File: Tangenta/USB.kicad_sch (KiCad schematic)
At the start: 29 parts, among them J12 907-211A1019D10200, J13 906-861A2116D10210, U8 USB2514B-I_M2, X1 X322524MOB4SI

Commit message: USB - current progress...
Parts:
- FB1: footprint footprint:L0805 -> Ferrite_Bead_100:Ferrite_Bead_100
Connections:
- net USB_U_N renamed USB_UP.N
- net USB_U_P renamed USB_UP.P
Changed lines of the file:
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@@
   (junction (at 38.862 173.609) (diameter 0) (color 0 0 0 0)
   )
-  (bus_entry (at 63.5 189.23) (size 2.54 2.54)
-    (stroke (width 0) (type default))
-  )
-  (bus_entry (at 54.61 189.23) (size 2.54 2.54)
+  (bus_entry (at 33.02 133.985) (size 2.54 2.54)
+    (stroke (width 0) (type default))
+  )
+  (bus_entry (at 41.91 133.985) (size 2.54 2.54)
+    (stroke (width 0) (type default))
+  )
+  (bus_entry (at 41.91 146.685) (size 2.54 2.54)
+    (stroke (width 0) (type default))
+  )
+  (bus_entry (at 33.02 146.685) (size 2.54 2.54)
     (stroke (width 0) (type default))
   )
@@
     (stroke (width 0) (type default))
   )
+  (bus (pts (xy 44.45 136.525) (xy 50.165 136.525))
+    (stroke (width 0) (type default))
+  )
   (wire (pts (xy 245.745 69.85) (xy 255.905 69.85))
     (stroke (width 0) (type default))
@@
     (stroke (width 0) (type default))
   )
-  (wire (pts (xy 45.72 186.055) (xy 60.325 186.055))
+  (wire (pts (xy 24.13 143.51) (xy 38.735 143.51))
+    (stroke (width 0) (type default))
+  )
+  (wire (pts (xy 55.118 163.83) (xy 55.118 166.37))
+    (stroke (width 0) (type default))
+  )
+  (wire (pts (xy 245.745 72.39) (xy 255.905 72.39))
+    (stroke (width 0) (type default))
+  )
+  (wire (pts (xy 167.6402 90.17) (xy 201.295 90.17))
+    (stroke (width 0) (type default))
+  )
+  (wire (pts (xy 29.464 182.88) (xy 36.449 182.88))
+    (stroke (width 0) (type default))
+  )
+  (wire (pts (xy 63.5 59.69) (xy 71.12 59.69))
+    (stroke (width 0) (type default))
+  )
+  (wire (pts (xy 62.611 163.83) (xy 62.611 166.37))
+    (stroke (width 0) (type default))
+  )
+  (wire (pts (xy 71.12 62.23) (xy 33.655 62.23))
     (stroke (width 0) (type default))
   )
@@
     (stroke (width 0) (type default))
   )
-  (wire (pts (xy 55.118 163.83) (xy 55.118 166.37))
-    (stroke (width 0) (type default))
-  )
-  (wire (pts (xy 245.745 72.39) (xy 255.905 72.39))
-    (stroke (width 0) (type default))
-  )
-  (wire (pts (xy 167.6402 90.17) (xy 201.295 90.17))
-    (stroke (width 0) (type default))
-  )
-  (wire (pts (xy 29.464 182.88) (xy 36.449 182.88))
-    (stroke (width 0) (type default))
-  )
-  (wire (pts (xy 63.5 59.69) (xy 71.12 59.69))
-    (stroke (width 0) (type default))
-  )
-  (wire (pts (xy 62.611 163.83) (xy 62.611 166.37))
-    (stroke (width 0) (type default))
-  )
-  (wire (pts (xy 71.12 62.23) (xy 33.655 62.23))
-    (stroke (width 0) (type default))
-  )
   (wire (pts (xy 194.945 87.63) (xy 186.055 87.63))
     (stroke (width 0) (type default))
@@
     (stroke (width 0) (type default))
   )
-  (wire (pts (xy 63.5 189.23) (xy 60.325 186.055))
+  (wire (pts (xy 41.91 146.685) (xy 38.735 143.51))
     (stroke (width 0) (type default))
   )
@@
     (stroke (width 0) (type default))
   )
+  (bus (pts (xy 35.56 136.525) (xy 44.45 136.525))
+    (stroke (width 0) (type default))
+  )
   (wire (pts (xy 28.575 82.55) (xy 37.465 82.55))
     (stroke (width 0) (type default))
@@
     (stroke (width 0) (type default))
   )
-  (bus (pts (xy 57.15 191.77) (xy 66.04 191.77))
+  (bus (pts (xy 35.56 149.225) (xy 44.45 149.225))
     (stroke (width 0) (type default))
   )
@@
     (stroke (width 0) (type default))
   )
+  (wire (pts (xy 41.91 133.985) (xy 38.735 130.81))
+    (stroke (width 0) (type default))
+  )
   (wire (pts (xy 268.605 46.99) (xy 279.4 46.99))
     (stroke (width 0) (type default))
   )
+  (wire (pts (xy 24.13 130.81) (xy 38.735 130.81))
+    (stroke (width 0) (type default))
+  )
   (wire (pts (xy 55.118 163.83) (xy 62.611 163.83))
     (stroke (width 0) (type default))
@@
     (stroke (width 0) (type default))
   )
-  (bus (pts (xy 66.04 191.77) (xy 71.755 191.77))
+  (bus (pts (xy 44.45 149.225) (xy 50.165 149.225))
     (stroke (width 0) (type default))
   )
@@
     (stroke (width 0) (type default))
   )
+  (wire (pts (xy 24.13 133.985) (xy 33.02 133.985))
+    (stroke (width 0) (type default))
+  )
   (wire (pts (xy 201.295 96.52) (xy 201.295 97.79))
     (stroke (width 0) (type default))
@@
     (stroke (width 0) (type default))
   )
-  (wire (pts (xy 45.72 189.23) (xy 54.61 189.23))
+  (wire (pts (xy 24.13 146.685) (xy 33.02 146.685))
     (stroke (width 0) (type default))
   )
@@
     (effects (font (size 1.27 1.27)) (justify right bottom))
   )
-  (label "USB_U_N" (at 60.325 72.39 0) (fields_autoplaced)
+  (label "USB_UP.N" (at 60.325 72.39 0) (fields_autoplaced)
     (effects (font (size 1.27 1.27)) (justify left bottom))
   )
@@
     (effects (font (size 1.27 1.27)) (justify left bottom))
   )
+  (label "USB_UP.P" (at 24.13 130.81 0) (fields_autoplaced)
+    (effects (font (size 1.27 1.27)) (justify left bottom))
+  )
   (label "3V3A" (at 177.8 80.01 180) (fields_autoplaced)
     (effects (font (size 1.27 1.27)) (justify right bottom))
@@
     (effects (font (size 1.27 1.27)) (justify left bottom))
   )
-  (label "USB_U_P" (at 60.325 69.85 0) (fields_autoplaced)
+  (label "USB_UP.P" (at 60.325 69.85 0) (fields_autoplaced)
     (effects (font (size 1.27 1.27)) (justify left bottom))
   )
@@
     (effects (font (size 1.27 1.27)) (justify left bottom))
   )
-  (label "USB_MODEM.N" (at 45.72 189.23 0) (fields_autoplaced)
+  (label "USB_MODEM.N" (at 24.13 146.685 0) (fields_autoplaced)
     (effects (font (size 1.27 1.27)) (justify left bottom))
   )
@@
     (effects (font (size 1.27 1.27)) (justify right bottom))
   )
+  (label "USB_UP.N" (at 24.13 133.985 0) (fields_autoplaced)
+    (effects (font (size 1.27 1.27)) (justify left bottom))
+  )
   (label "3V3" (at 28.575 82.55 0) (fields_autoplaced)
     (effects (font (size 1.27 1.27)) (justify left bottom))
@@
     (effects (font (size 1.27 1.27)) (justify right bottom))
   )
-  (label "USB_MODEM.P" (at 45.72 186.055 0) (fields_autoplaced)
+  (label "USB_MODEM.P" (at 24.13 143.51 0) (fields_autoplaced)
     (effects (font (size 1.27 1.27)) (justify left bottom))
   )
@@
     (effects (font (size 1.27 1.27)) (justify right))
   )
-  (hierarchical_label "USB_MODEM{P N}" (shape output) (at 71.755 191.77 0) (fields_autoplaced)
+  (hierarchical_label "USB_MODEM{P N}" (shape output) (at 50.165 149.225 0) (fields_autoplaced)
     (effects (font (size 1.27 1.27)) (justify left))
   )
@@
   (hierarchical_label "3V3" (shape input) (at 29.083 163.83 180) (fields_autoplaced)
     (effects (font (size 1.27 1.27)) (justify right))
+  )
+  (hierarchical_label "USB_UP{P N}" (shape input) (at 50.165 136.525 0) (fields_autoplaced)
+    (effects (font (size 1.27 1.27)) (justify left))
   )
   (hierarchical_label "CHASSIS" (shape bidirectional) (at 28.702 192.024 180) (fields_autoplaced)
@@
         (path "/358d1bcf-7599-4352-8c4d-baa18a5f09e6/b1871a4d-6a35-44e2-a9a2-9a4af684371d"
           (reference "#PWR033") (unit 1)
-        )
-      )
-    )
-  )
-  (symbol (lib_id "Ferrite_Bead_100:GZ2012D101TF") (at 50.673 163.83 0) (unit 1)
-    (in_bom yes) (on_board yes) (dnp no)
-    (property "Reference" "FB1" (at 50.038 161.29 0)
-      (effects (font (size 1.27 1.27)))
-    )
-    (property "Value" "GZ2012D101TF" (at 50.673 160.02 0)
-      (effects (font (size 1.27 1.27)) hide)
-    )
-    (property "Footprint" "footprint:L0805" (at 53.848 173.99 0)
-      (effects (font (size 1.27 1.27) italic) hide)
-    )
-    (property "Datasheet" "https://item.szlcsc.com/344132.html" (at 46.482 171.577 0)
-      (effects (font (size 1.27 1.27)) (justify left) hide)
-    )
-    (property "LCSC" "C1015" (at 49.53 167.259 0)
-      (effects (font (size 1.27 1.27)) hide)
-    )
-    (pin "1")
-    (pin "2")
-    (instances
-      (project "Tangenta"
-        (path "/358d1bcf-7599-4352-8c4d-baa18a5f09e6/b1871a4d-6a35-44e2-a9a2-9a4af684371d"
-          (reference "FB1") (unit 1)
         )
       )
@@
         )
       )
+    )
+  )
+  (symbol (lib_id "Ferrite_Bead_100:GZ2012D101TF") (at 50.673 163.83 0) (unit 1)
+    (in_bom yes) (on_board yes) (dnp no)
+    (property "Reference" "FB1" (at 50.673 161.29 0)
+      (effects (font (size 1.27 1.27)))
+    )
+    (property "Value" "GZ2012D101TF" (at 50.673 160.02 0)
+      (effects (font (size 1.27 1.27)) hide)
+    )
+    (property "Footprint" "Ferrite_Bead_100:Ferrite_Bead_100" (at 63.246 173.863 0)
+      (effects (font (size 1.27 1.27) italic) hide)
+    )
+    (property "Datasheet" "https://item.szlcsc.com/344132.html" (at 46.482 171.577 0)
+      (effects (font (size 1.27 1.27)) (justify left) hide)
+    )
+    (property "LCSC" "C1015" (at 49.53 167.259 0)
+      (effects (font (size 1.27 1.27)) hide)
+    )
+    (pin "1")
+    (pin "2")
+    (instances
+      (project "Tangenta"
+        (path "/358d1bcf-7599-4352-8c4d-baa18a5f09e6/b1871a4d-6a35-44e2-a9a2-9a4af684371d"
+          (reference "FB1") (unit 1)
+        )
+      )

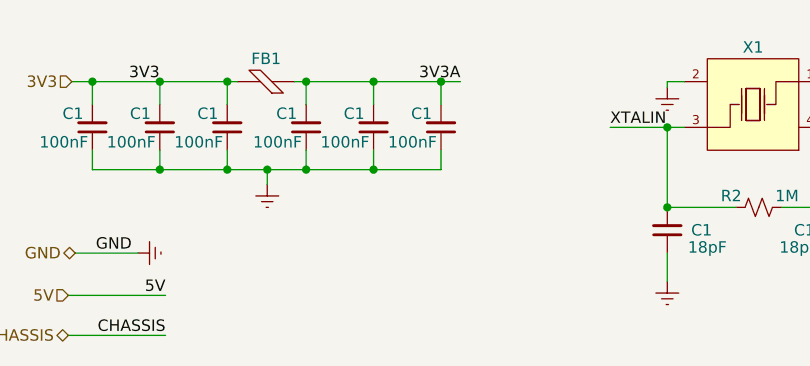
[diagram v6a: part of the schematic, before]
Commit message: USB routed.
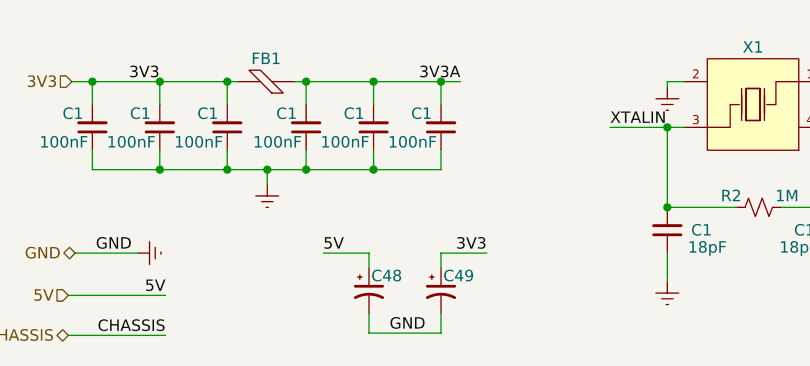
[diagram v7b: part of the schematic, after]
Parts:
- added C48, C49: 16CE47FSS, CAP_L5:CAP_L5, symbol CAP_L5:16CE47FSS
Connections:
- net 3V3: now also C49.1
- net 5V: now also C48.1
- net GNDREF: now also C48.2, C49.2
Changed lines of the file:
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@@
+    (stroke (width 0) (type default))
+  )
+  (wire (pts (xy 57.023 182.88) (xy 62.103 182.88))
     (stroke (width 0) (type default))
   )
@@
     (stroke (width 0) (type default))
   )
+  (wire (pts (xy 70.104 184.531) (xy 70.104 182.88))
+    (stroke (width 0) (type default))
+  )
   (wire (pts (xy 167.6402 77.47) (xy 189.23 77.47))
     (stroke (width 0) (type default))
@@
     (stroke (width 0) (type default))
   )
+  (wire (pts (xy 62.103 191.77) (xy 70.104 191.77))
+    (stroke (width 0) (type default))
+  )
   (wire (pts (xy 49.53 92.71) (xy 58.42 92.71))
     (stroke (width 0) (type default))
@@
     (stroke (width 0) (type default))
   )
+  (wire (pts (xy 62.103 189.611) (xy 62.103 191.77))
+    (stroke (width 0) (type default))
+  )
   (wire (pts (xy 38.862 173.609) (xy 46.355 173.609))
     (stroke (width 0) (type default))
@@
     (stroke (width 0) (type default))
   )
+  (wire (pts (xy 75.184 182.88) (xy 70.104 182.88))
+    (stroke (width 0) (type default))
+  )
   (wire (pts (xy 31.369 163.83) (xy 31.369 166.37))
     (stroke (width 0) (type default))
@@
     (stroke (width 0) (type default))
   )
+  (wire (pts (xy 62.103 184.531) (xy 62.103 182.88))
+    (stroke (width 0) (type default))
+  )
   (wire (pts (xy 245.745 64.77) (xy 255.905 64.77))
     (stroke (width 0) (type default))
@@
     (stroke (width 0) (type default))
   )
+  (wire (pts (xy 70.104 191.77) (xy 70.104 189.611))
+    (stroke (width 0) (type default))
+  )
   (wire (pts (xy 167.6402 82.55) (xy 177.8 82.55))
     (stroke (width 0) (type default))
@@
     (effects (font (size 1.27 1.27)) (justify left bottom))
   )
+  (label "3V3" (at 75.184 182.88 180) (fields_autoplaced)
+    (effects (font (size 1.27 1.27)) (justify right bottom))
+  )
   (label "3V3" (at 63.5 90.17 0) (fields_autoplaced)
     (effects (font (size 1.27 1.27)) (justify left bottom))
@@
     (effects (font (size 1.27 1.27)) (justify right bottom))
   )
+  (label "GND" (at 64.389 191.77 0) (fields_autoplaced)
+    (effects (font (size 1.27 1.27)) (justify left bottom))
+  )
   (label "GND" (at 49.53 77.47 0) (fields_autoplaced)
     (effects (font (size 1.27 1.27)) (justify left bottom))
@@
   )
   (label "3V3" (at 28.575 97.79 0) (fields_autoplaced)
+    (effects (font (size 1.27 1.27)) (justify left bottom))
+  )
+  (label "5V" (at 57.023 182.88 0) (fields_autoplaced)
     (effects (font (size 1.27 1.27)) (justify left bottom))
   )
@@
     )
   )
+  (symbol (lib_id "CAP_L5:16CE47FSS") (at 62.103 187.071 0) (unit 1)
+    (in_bom yes) (on_board yes) (dnp no)
+    (property "Reference" "C48" (at 62.357 185.42 0)
+      (effects (font (size 1.27 1.27)) (justify left))
+    )
+    (property "Value" "16CE47FSS" (at 64.516 187.9092 0)
+      (effects (font (size 1.27 1.27)) (justify left) hide)
+    )
+    (property "Footprint" "CAP_L5:CAP_L5" (at 60.833 204.851 0)
+      (effects (font (size 1.27 1.27) italic) hide)
+    )
+    (property "Datasheet" "https://item.szlcsc.com/245725.html" (at 53.721 202.565 0)
+      (effects (font (size 1.27 1.27)) (justify left) hide)
+    )
+    (property "LCSC" "C242026" (at 58.039 200.279 0)
+      (effects (font (size 1.27 1.27)) hide)
+    )
+    (property "Capacitance" "47uF" (at 66.675 187.325 0)
+      (effects (font (size 1.27 1.27)) hide)
+    )
+    (pin "1")
+    (pin "2")
+    (instances
+      (project "Tangenta"
+        (path "/358d1bcf-7599-4352-8c4d-baa18a5f09e6/b1871a4d-6a35-44e2-a9a2-9a4af684371d"
+          (reference "C48") (unit 1)
+        )
+      )
+    )
+  )
   (symbol (lib_id "Device:R_Small_US") (at 105.41 177.8 90) (unit 1)
     (in_bom yes) (on_board yes) (dnp no)
@@
         )
       )
+    )
+  )
+  (symbol (lib_id "CAP_L5:16CE47FSS") (at 70.104 187.071 0) (unit 1)
+    (in_bom yes) (on_board yes) (dnp no)
+    (property "Reference" "C49" (at 70.358 185.42 0)
+      (effects (font (size 1.27 1.27)) (justify left))
+    )
+    (property "Value" "16CE47FSS" (at 72.517 187.9092 0)
+      (effects (font (size 1.27 1.27)) (justify left) hide)
+    )
+    (property "Footprint" "CAP_L5:CAP_L5" (at 68.834 204.851 0)
+      (effects (font (size 1.27 1.27) italic) hide)
+    )
+    (property "Datasheet" "https://item.szlcsc.com/245725.html" (at 61.722 202.565 0)
+      (effects (font (size 1.27 1.27)) (justify left) hide)
+    )
+    (property "LCSC" "C242026" (at 66.04 200.279 0)
+      (effects (font (size 1.27 1.27)) hide)
+    )
+    (property "Capacitance" "47uF" (at 74.676 187.325 0)
+      (effects (font (size 1.27 1.27)) hide)
+    )
+    (pin "1")
+    (pin "2")
+    (instances
+      (project "Tangenta"
+        (path "/358d1bcf-7599-4352-8c4d-baa18a5f09e6/b1871a4d-6a35-44e2-a9a2-9a4af684371d"
+          (reference "C49") (unit 1)
+        )
+      )

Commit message: ...
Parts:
- removed J13: 906-861A2116D10210, USB_VERTICAL:USB_Vertical, symbol USB_VERTICAL:906-861A2116D10210
- added J13: 906-151A1058D10200, USB_VERTICAL_BLUE:USB_VERTICAL_BLUE, symbol USB_VERTICAL_BLUE:906-151A1058D10200
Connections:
- net 5V: now also J13.1 (VCC)
- net CHASSIS: now also J13.5 (SHELL), J13.6 (SHELL), J13.7 (SHELL)
- net GNDREF: now also J13.4 (GND)
- net USB_D3_N: now also J13.2 (D-)
- net USB_D3_P: now also J13.3 (D+)
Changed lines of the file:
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@@
   (junction (at 114.3 177.8) (diameter 0) (color 0 0 0 0)
   )
+  (junction (at 279.4 88.9) (diameter 0) (color 0 0 0 0)
+  )
   (junction (at 95.25 168.91) (diameter 0) (color 0 0 0 0)
   )
@@
     (stroke (width 0) (type default))
   )
-  (wire (pts (xy 276.225 95.885) (xy 283.845 95.885))
+  (wire (pts (xy 276.86 96.52) (xy 284.48 96.52))
     (stroke (width 0) (type default))
   )
@@
     (stroke (width 0) (type default))
   )
-  (wire (pts (xy 276.225 88.265) (xy 283.845 88.265))
+  (wire (pts (xy 276.86 88.9) (xy 279.4 88.9))
     (stroke (width 0) (type default))
   )
@@
     (stroke (width 0) (type default))
   )
+  (wire (pts (xy 276.86 91.44) (xy 279.4 91.44))
+    (stroke (width 0) (type default))
+  )
   (wire (pts (xy 49.53 85.09) (xy 58.42 85.09))
     (stroke (width 0) (type default))
@@
     (stroke (width 0) (type default))
   )
-  (wire (pts (xy 245.745 95.885) (xy 255.905 95.885))
+  (wire (pts (xy 246.38 96.52) (xy 256.54 96.52))
     (stroke (width 0) (type default))
   )
@@
     (stroke (width 0) (type default))
   )
-  (wire (pts (xy 245.745 88.265) (xy 255.905 88.265))
+  (wire (pts (xy 246.38 88.9) (xy 256.54 88.9))
     (stroke (width 0) (type default))
   )
@@
     (stroke (width 0) (type default))
   )
-  (wire (pts (xy 245.745 90.805) (xy 255.905 90.805))
+  (wire (pts (xy 246.38 91.44) (xy 256.54 91.44))
     (stroke (width 0) (type default))
   )
@@
     (stroke (width 0) (type default))
   )
+  (wire (pts (xy 279.4 88.9) (xy 284.48 88.9))
+    (stroke (width 0) (type default))
+  )
   (wire (pts (xy 48.895 59.69) (xy 58.42 59.69))
     (stroke (width 0) (type default))
@@
     (stroke (width 0) (type default))
   )
-  (wire (pts (xy 245.745 93.345) (xy 255.905 93.345))
+  (wire (pts (xy 246.38 93.98) (xy 256.54 93.98))
     (stroke (width 0) (type default))
   )
@@
     (stroke (width 0) (type default))
   )
+  (wire (pts (xy 279.4 91.44) (xy 279.4 88.9))
+    (stroke (width 0) (type default))
+  )
   (wire (pts (xy 245.745 64.77) (xy 255.905 64.77))
     (stroke (width 0) (type default))
@@
     (effects (font (size 1.27 1.27)) (justify left bottom))
   )
-  (label "CHASSIS" (at 283.845 95.885 180) (fields_autoplaced)
-    (effects (font (size 1.27 1.27)) (justify right bottom))
-  )
-  (label "GND" (at 245.745 95.885 0) (fields_autoplaced)
+  (label "CHASSIS" (at 284.48 96.52 180) (fields_autoplaced)
+    (effects (font (size 1.27 1.27)) (justify right bottom))
+  )
+  (label "GND" (at 246.38 96.52 0) (fields_autoplaced)
     (effects (font (size 1.27 1.27)) (justify left bottom))
   )
@@
     (effects (font (size 1.27 1.27)) (justify right bottom))
   )
-  (label "USB_D3_N" (at 245.745 90.805 0) (fields_autoplaced)
+  (label "USB_D3_N" (at 246.38 91.44 0) (fields_autoplaced)
     (effects (font (size 1.27 1.27)) (justify left bottom))
   )
@@
     (effects (font (size 1.27 1.27)) (justify right bottom))
   )
-  (label "USB_D3_P" (at 245.745 93.345 0) (fields_autoplaced)
+  (label "USB_D3_P" (at 246.38 93.98 0) (fields_autoplaced)
     (effects (font (size 1.27 1.27)) (justify left bottom))
   )
@@
     (effects (font (size 1.27 1.27)) (justify left bottom))
   )
-  (label "5V" (at 245.745 88.265 0) (fields_autoplaced)
+  (label "5V" (at 246.38 88.9 0) (fields_autoplaced)
     (effects (font (size 1.27 1.27)) (justify left bottom))
   )
@@
     (effects (font (size 1.27 1.27)) (justify left bottom))
   )
-  (label "CHASSIS" (at 283.845 88.265 180) (fields_autoplaced)
+  (label "CHASSIS" (at 284.48 88.9 180) (fields_autoplaced)
     (effects (font (size 1.27 1.27)) (justify right bottom))
   )
@@
     )
   )
-  (symbol (lib_id "USB_VERTICAL:906-861A2116D10210") (at 266.065 90.805 0) (unit 1)
-    (in_bom yes) (on_board yes) (dnp no)
-    (property "Reference" "J13" (at 260.35 83.82 0)
-      (effects (font (size 1.27 1.27)))
-    )
-    (property "Value" "906-861A2116D10210" (at 266.065 83.82 0)
-      (effects (font (size 1.27 1.27)) hide)
-    )
-    (property "Footprint" "USB_VERTICAL:USB_Vertical" (at 269.875 106.045 0)
-      (effects (font (size 1.27 1.27) italic) hide)
-    )
-    (property "Datasheet" "https://atta.szlcsc.com/upload/public/pdf/source/20210526/C2763350_E0D561271332FF88E1B9AF264603FE9E.pdf" (at 257.175 108.585 0)
-      (effects (font (size 1.27 1.27)) (justify left) hide)
-    )
-    (property "LCSC" "C2763350" (at 262.255 103.505 0)
-      (effects (font (size 1.27 1.27)) hide)
-    )
-    (pin "1")
-    (pin "2")
-    (pin "3")
-    (pin "4")
-    (pin "5")
-    (pin "6")
-    (instances
-      (project "Tangenta"
-        (path "/358d1bcf-7599-4352-8c4d-baa18a5f09e6/b1871a4d-6a35-44e2-a9a2-9a4af684371d"
-          (reference "J13") (unit 1)
-        )
-      )
-    )
-  )
   (symbol (lib_id "Device:C_Small") (at 206.375 93.98 180) (unit 1)
     (in_bom yes) (on_board yes) (dnp no)
@@
         )
       )
+    )
+  )
+  (symbol (lib_id "USB_VERTICAL_BLUE:906-151A1058D10200") (at 266.7 93.98 0) (unit 1)
+    (in_bom yes) (on_board yes) (dnp no)
+    (property "Reference" "J13" (at 260.35 85.09 0)
+      (effects (font (size 1.27 1.27)))
+    )
+    (property "Value" "906-151A1058D10200" (at 266.7 100.33 0)
+      (effects (font (size 1.27 1.27)) hide)
+    )
+    (property "Footprint" "USB_VERTICAL_BLUE:USB_VERTICAL_BLUE" (at 267.589 108.585 0)
+      (effects (font (size 1.27 1.27) italic) hide)
+    )
+    (property "Datasheet" "https://item.szlcsc.com/2892439.html" (at 248.539 106.299 0)
+      (effects (font (size 1.27 1.27)) (justify left) hide)
+    )
+    (property "LCSC" "C2763227" (at 253.492 104.267 0)
+      (effects (font (size 1.27 1.27)) hide)
+    )
+    (pin "1")
+    (pin "2")
+    (pin "3")
+    (pin "4")
+    (pin "5")
+    (pin "6")
+    (pin "7")
+    (instances
+      (project "Tangenta"
+        (path "/358d1bcf-7599-4352-8c4d-baa18a5f09e6/b1871a4d-6a35-44e2-a9a2-9a4af684371d"
+          (reference "J13") (unit 1)
+        )
+      )
